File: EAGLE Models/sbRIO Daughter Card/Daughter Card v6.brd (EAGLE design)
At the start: 153.7 x 102.9 mm, 96 parts, among them IC1 BTS716G, IC2 BTS716G, IC3 BTS716G

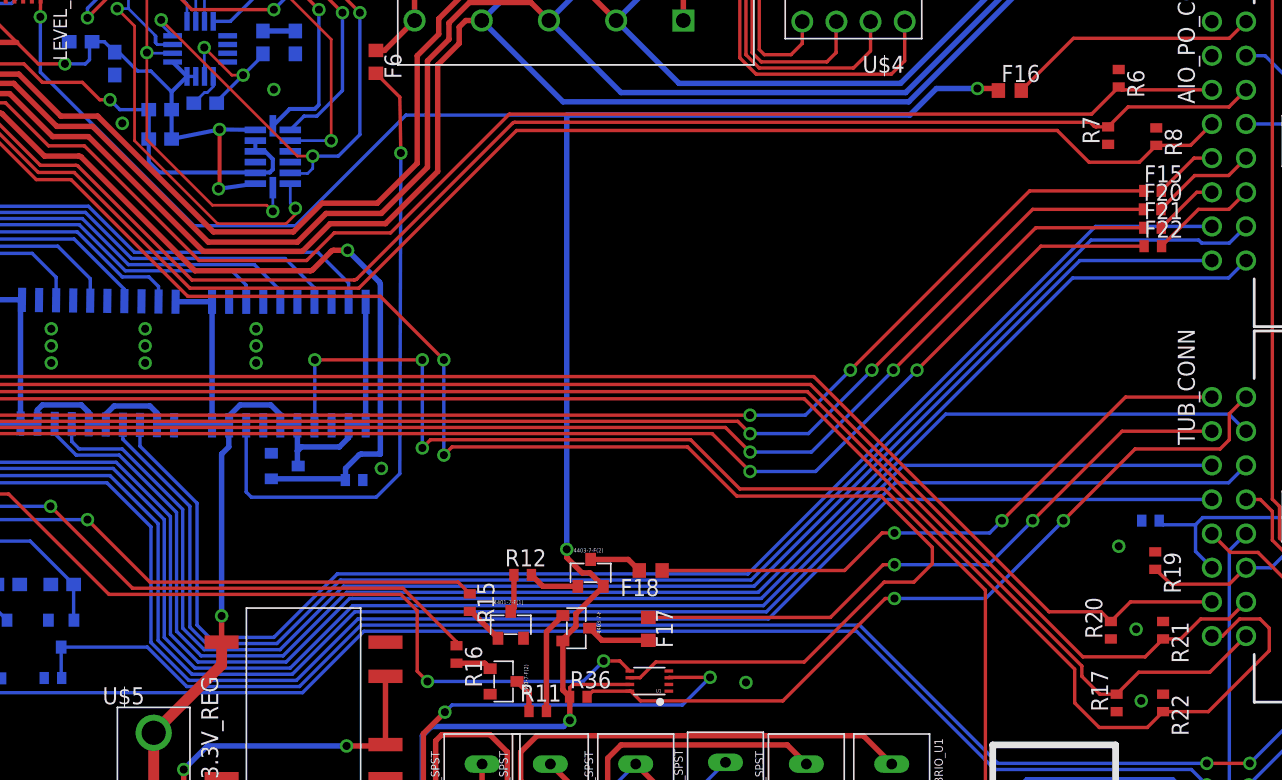
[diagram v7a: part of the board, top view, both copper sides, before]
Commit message: fixed more ground connections
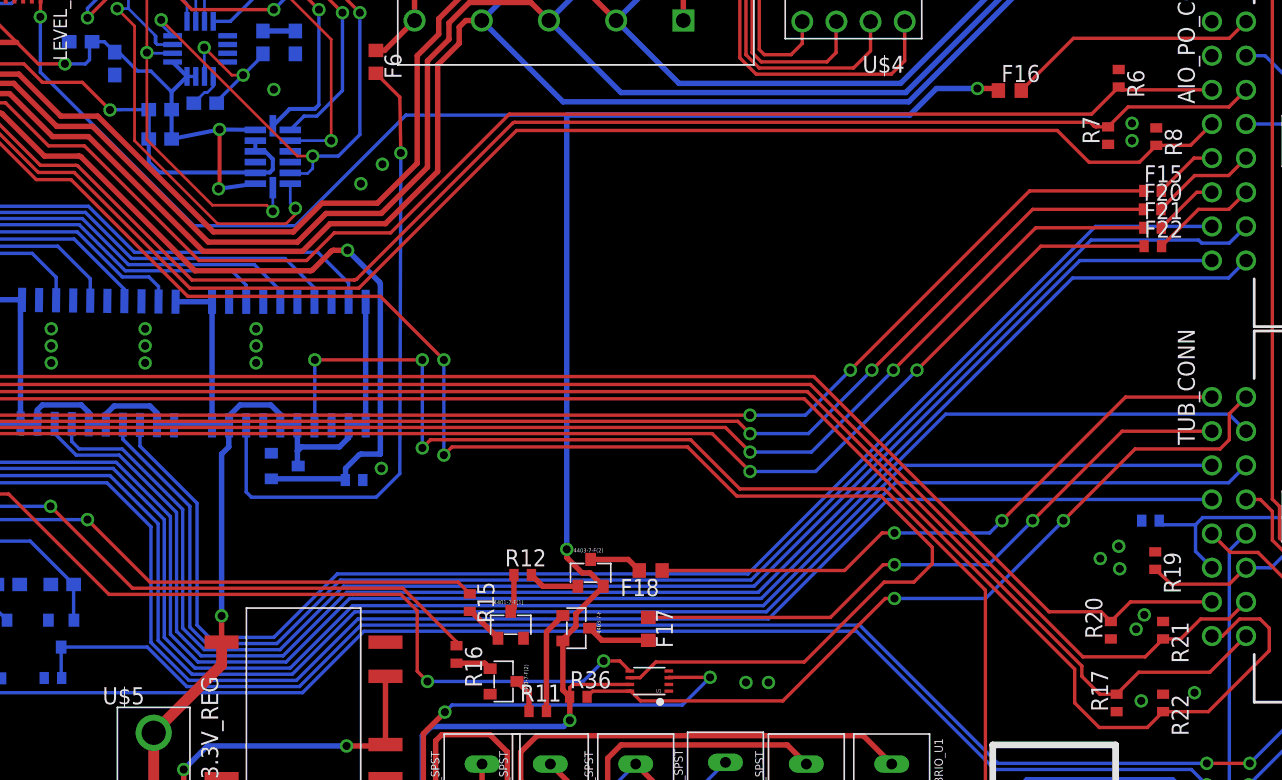
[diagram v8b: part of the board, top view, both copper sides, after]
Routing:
- net GND: vias 26 -> 34
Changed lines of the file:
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@@
 <via x="69.85" y="66.04" extent="1-16" drill="0.6"/>
 <via x="69.85" y="64.77" extent="1-16" drill="0.6"/>
-<via x="59.8932" y="82.6008" extent="1-16" drill="0.6"/>
+<via x="77.6478" y="78.105" extent="1-16" drill="0.6"/>
+<via x="79.248" y="79.5528" extent="1-16" drill="0.6"/>
+<via x="135.0264" y="82.6008" extent="1-16" drill="0.6"/>
+<via x="135.0264" y="81.3054" extent="1-16" drill="0.6"/>
+<via x="134.112" y="49.4538" extent="1-16" drill="0.6"/>
+<via x="132.6642" y="50.2158" extent="1-16" drill="0.6"/>
+<via x="107.9754" y="40.9956" extent="1-16" drill="0.6"/>
+<via x="135.9408" y="46.0248" extent="1-16" drill="0.6"/>
+<via x="139.6746" y="40.2336" extent="1-16" drill="0.6"/>
 <wire x1="20.1318" y1="60.6044" x2="20.1318" y2="58.5724" width="0" layer="19" extent="16-16"/>
 <wire x1="20.1318" y1="63.246" x2="20.1318" y2="60.6044" width="0" layer="19" extent="16-16"/>
-<wire x1="65.2154" y1="84.0994" x2="59.8932" y2="82.6008" width="0" layer="19" extent="16-16"/>
-<wire x1="136.8298" y1="82.2602" x2="134.0358" y2="86.6036" width="0" layer="19" extent="1-1"/>
 </signal>
 <signal name="12V">
@@
 <wire x1="52.578" y1="87.0204" x2="53.9496" y2="85.6488" width="0.254" layer="1"/>
 <wire x1="53.9496" y1="85.6488" x2="56.9214" y2="85.6488" width="0.254" layer="1"/>
-<wire x1="56.9214" y1="85.6488" x2="58.2168" y2="84.3534" width="0.254" layer="1"/>
-<wire x1="58.2168" y1="84.3534" x2="58.9788" y2="84.3534" width="0.254" layer="1"/>
-<via x="58.9788" y="84.3534" extent="1-16" drill="0.6"/>
-<wire x1="58.9788" y1="84.3534" x2="59.7154" y2="83.6168" width="0.254" layer="16"/>
+<wire x1="56.9214" y1="85.6488" x2="58.9788" y2="83.5914" width="0.254" layer="1"/>
+<via x="58.9788" y="83.5914" extent="1-16" drill="0.6"/>
+<wire x1="58.9788" y1="83.5914" x2="59.7154" y2="83.6168" width="0.254" layer="16"/>
 <wire x1="59.7154" y1="83.6168" x2="61.8626" y2="83.6168" width="0.254" layer="16"/>
 <wire x1="30.067" y1="59.756" x2="29.1084" y2="58.7974" width="0.254" layer="16"/>
